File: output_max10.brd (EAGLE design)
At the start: 73.9 x 54.2 mm, 56 parts, among them IC4 IS61WV1288EEBLL-10HLI, IC5 10M04EQFP144

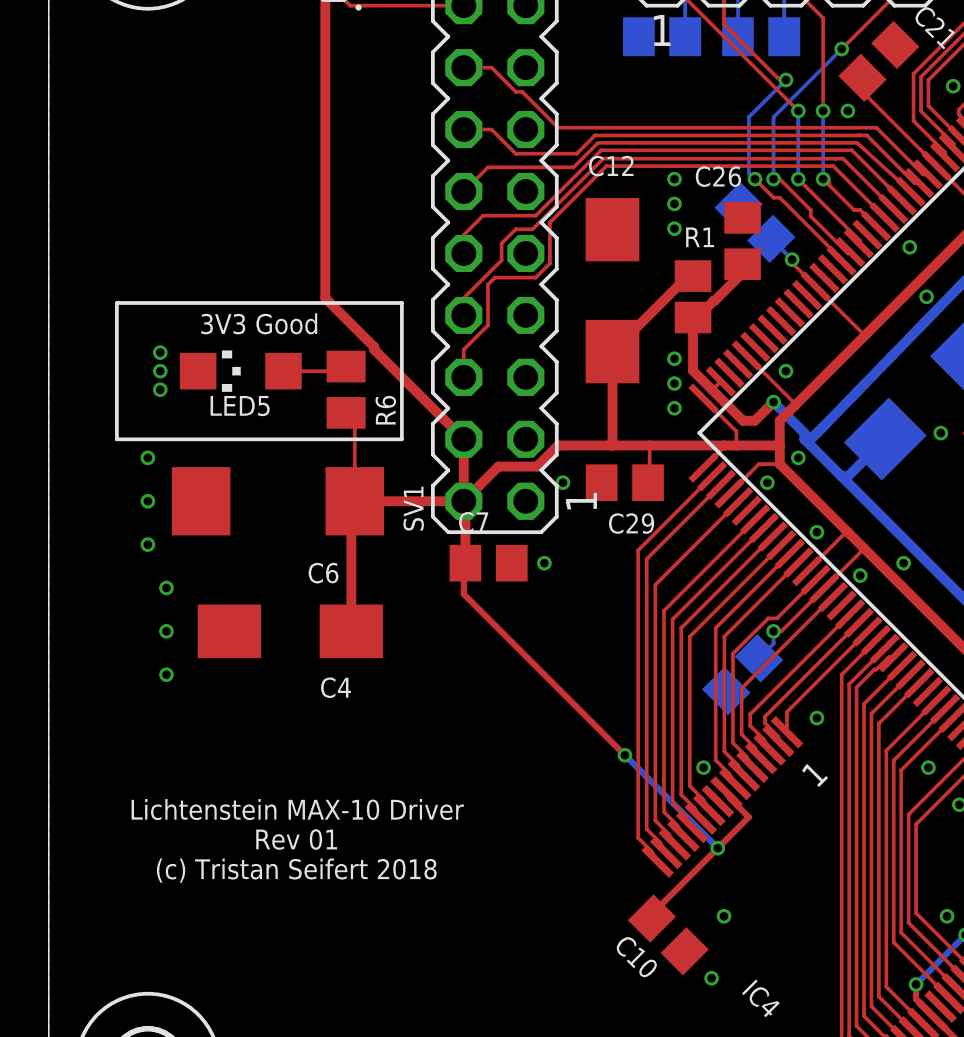
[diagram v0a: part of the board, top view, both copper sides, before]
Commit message: Added clock generator to FPGA (lol)
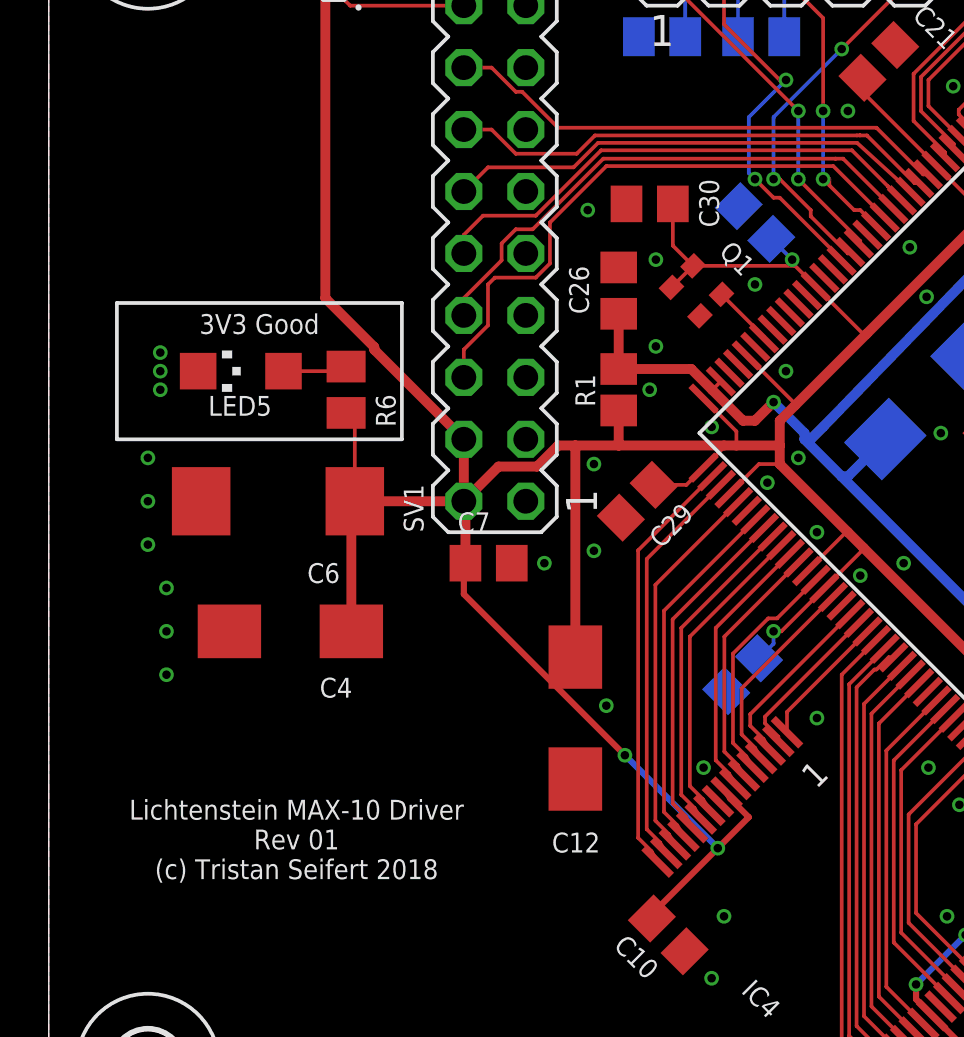
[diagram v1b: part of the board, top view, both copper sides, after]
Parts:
- added C30: 100nF, rcl:C0805
- added Q1: (no value), lichtenstein_onion:VLGA-4
- moved C12 17.6 mm to (21.6, 18.3), turned to 270 degrees
- moved C26 5.47 mm to (23.4, 35.8)
- moved R1 4.88 mm to (23.4, 31.8), turned to 90 degrees
- moved C29 0.92 mm to (24.1, 27.2), turned to 225 degrees
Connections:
- net +3V3: now also C30.1, Q1.1, Q1.4
- net CLKIN_24: now also IC5.29, Q1.3; no longer IC5.27
- net GND: now also C30.2, Q1.2
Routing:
- net +3V3: track 327.4 -> 338.2 mm
- net CLKIN_24: track 0.00 -> 2.52 mm
